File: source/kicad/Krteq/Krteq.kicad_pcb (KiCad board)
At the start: 2 copper layers, 228.6 x 116.3 mm, 263 parts, among them Q1 Q_NMOS_GSD, Q2 Q_NMOS_GSD, Q3 Q_NMOS_GSD, Q4 Q_NMOS_GSD, SW1 Switch, SW10 Switch, SW11 Switch, SW12 Switch, SW13 Switch, SW14 Switch, SW15 Switch, SW16 Switch, SW17 Switch, SW18 Switch, SW19 Switch, SW2 Switch, SW20 Switch, SW21 Switch, SW22 Switch, SW23 Switch, SW24 Switch, SW25 Switch, SW26 Switch, SW27 Switch, SW28 Switch, SW29 Switch, SW3 Switch, SW30 Switch, SW31 Switch, SW32 Switch, SW33 Switch, SW34 Switch, SW35 Switch, SW36 Switch, SW37 Switch, SW38 Switch, SW39 Switch, SW4 Switch, SW40 Switch, SW41 Switch, SW42 Switch, SW43 Switch, SW44 Switch, SW45 Switch, SW46 Switch, SW47 Switch, SW48 Switch, SW49 Switch, SW5 Switch, SW50 Switch, SW51 Switch, SW52 Switch, SW53 Switch, SW54 Switch, SW55 Switch, SW56 Switch, SW57 Switch, SW58 Switch, SW59 Switch, SW6 Switch, SW60 Switch, SW61 Switch, SW7 Switch, SW8 Switch, SW9 Switch

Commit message: MCU cable distance
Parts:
- moved A1 15.0 mm to (204.7, 95.5)
- moved R10 11.1 mm to (144.5, 79.8), turned to -90 degrees
- moved Q4 8.99 mm to (138.6, 79.8), turned to 180 degrees
- moved R11 4.54 mm to (133.0, 79.8), turned to -90 degrees
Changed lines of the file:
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@@
 	(footprint "Resistor_SMD:R_0603_1608Metric"
 		(layer "B.Cu")
-		(at 128.425 79.548 180)
+		(at 132.9625 79.7855 -90)
 		(descr "Resistor SMD 0603 (1608 Metric), square (rectangular) end terminal, IPC-7351 nominal, (Body size source: IPC-SM-782 page 72, https://www.pcb-3d.com/wordpress/wp-content/uploads/ipc-sm-782a_amendment_1_and_2.pdf), generated with kicad-footprint-generator")
 		(tags "resistor")
 		(property "Reference" "R11"
-			(at 0 1.43 0)
+			(at 0 1.43 90)
 			(layer "B.SilkS")
 			(effects
@@
 		)
 		(property "Value" "10k"
-			(at 0 -1.43 0)
+			(at 0 -1.43 90)
 			(layer "B.Fab")
 			(effects
@@
 		)
 		(property "Datasheet" "~"
-			(at 0 0 0)
+			(at 0 0 90)
 			(layer "B.Fab")
 			(hide yes)
@@
 		)
 		(property "Description" "Resistor"
-			(at 0 0 0)
+			(at 0 0 90)
 			(layer "B.Fab")
 			(hide yes)
@@
 		)
 		(fp_text user "${REFERENCE}"
-			(at 0 0 0)
+			(at 0 0 90)
 			(layer "B.Fab")
 			(effects
@@
 		)
 		(pad "1" smd roundrect
-			(at -0.825 0 180)
+			(at -0.825 0 270)
 			(size 0.8 0.95)
 			(layers "B.Cu" "B.Mask" "B.Paste")
@@
 		)
 		(pad "2" smd roundrect
-			(at 0.825 0 180)
+			(at 0.825 0 270)
 			(size 0.8 0.95)
 			(layers "B.Cu" "B.Mask" "B.Paste")
@@
 	(footprint "Package_TO_SOT_SMD:SOT-23"
 		(layer "B.Cu")
-		(at 130.925 84.548 -90)
+		(at 138.55 79.7855 180)
 		(descr "SOT, 3 Pin (JEDEC TO-236 Var AB https://www.jedec.org/document_search?search_api_views_fulltext=TO-236), generated with kicad-footprint-generator ipc_gullwing_generator.py")
 		(tags "SOT TO_SOT_SMD")
 		(property "Reference" "Q4"
-			(at 0 2.4 90)
+			(at 0 2.4 0)
 			(layer "B.SilkS")
 			(effects
@@
 		)
 		(property "Value" "Q_NMOS_GSD"
-			(at 0 -2.4 90)
+			(at 0 -2.4 0)
 			(layer "B.Fab")
 			(effects
@@
 		)
 		(property "Datasheet" "~"
-			(at 0 0 90)
+			(at 0 0 0)
 			(layer "B.Fab")
 			(hide yes)
@@
 		)
 		(property "Description" "N-MOSFET transistor, gate/source/drain"
-			(at 0 0 90)
+			(at 0 0 0)
 			(layer "B.Fab")
 			(hide yes)
@@
 		(attr smd)
 		(fp_line
-			(start -0.76 1.56)
-			(end 0.76 1.56)
+			(start 0.76 1.56)
+			(end 0.76 0.56)
 			(stroke
 				(width 0.12)
@@
 		)
 		(fp_line
-			(start 0.76 1.56)
-			(end 0.76 0.56)
+			(start 0.76 -0.56)
+			(end 0.76 -1.56)
 			(stroke
 				(width 0.12)
@@
 		)
 		(fp_line
-			(start -0.76 1.51)
-			(end -0.76 1.56)
+			(start 0.76 -1.56)
+			(end -0.76 -1.56)
 			(stroke
 				(width 0.12)
@@
 		)
 		(fp_line
-			(start -0.76 -0.39)
-			(end -0.76 0.39)
+			(start -0.76 1.56)
+			(end 0.76 1.56)
 			(stroke
 				(width 0.12)
@@
 		)
 		(fp_line
-			(start 0.76 -0.56)
-			(end 0.76 -1.56)
+			(start -0.76 1.51)
+			(end -0.76 1.56)
 			(stroke
 				(width 0.12)
@@
 		)
 		(fp_line
-			(start -0.76 -1.56)
-			(end -0.76 -1.51)
+			(start -0.76 -0.39)
+			(end -0.76 0.39)
 			(stroke
 				(width 0.12)
@@
 		)
 		(fp_line
-			(start 0.76 -1.56)
-			(end -0.76 -1.56)
+			(start -0.76 -1.56)
+			(end -0.76 -1.51)
 			(stroke
 				(width 0.12)
@@
 		)
 		(fp_line
-			(start -0.9 1.7)
-			(end 0.9 1.7)
+			(start 1.93 0.55)
+			(end 1.93 -0.55)
 			(stroke
 				(width 0.05)
@@
 		)
 		(fp_line
-			(start 0.9 1.7)
-			(end 0.9 0.55)
+			(start 1.93 -0.55)
+			(end 0.9 -0.55)
 			(stroke
 				(width 0.05)
@@
 		)
 		(fp_line
-			(start -1.93 1.5)
-			(end -0.9 1.5)
+			(start 0.9 1.7)
+			(end 0.9 0.55)
 			(stroke
 				(width 0.05)
@@
 		)
 		(fp_line
-			(start -0.9 1.5)
-			(end -0.9 1.7)
+			(start 0.9 0.55)
+			(end 1.93 0.55)
 			(stroke
 				(width 0.05)
@@
 		)
 		(fp_line
-			(start 0.9 0.55)
-			(end 1.93 0.55)
+			(start 0.9 -0.55)
+			(end 0.9 -1.7)
 			(stroke
 				(width 0.05)
@@
 		)
 		(fp_line
-			(start 1.93 0.55)
-			(end 1.93 -0.55)
+			(start 0.9 -1.7)
+			(end -0.9 -1.7)
 			(stroke
 				(width 0.05)
@@
 		)
 		(fp_line
-			(start -1.93 0.39)
-			(end -1.93 1.5)
+			(start -0.9 1.7)
+			(end 0.9 1.7)
 			(stroke
 				(width 0.05)
@@
 		)
 		(fp_line
-			(start -0.9 0.39)
-			(end -1.93 0.39)
+			(start -0.9 1.5)
+			(end -0.9 1.7)
 			(stroke
 				(width 0.05)
@@
 		)
 		(fp_line
-			(start -1.93 -0.39)
-			(end -0.9 -0.39)
+			(start -0.9 0.39)
+			(end -1.93 0.39)
 			(stroke
 				(width 0.05)
@@
 		)
 		(fp_line
-			(start 0.9 -0.55)
-			(end 0.9 -1.7)
+			(start -0.9 -1.5)
+			(end -1.93 -1.5)
 			(stroke
 				(width 0.05)
@@
 		)
 		(fp_line
-			(start 1.93 -0.55)
-			(end 0.9 -0.55)
+			(start -0.9 -1.7)
+			(end -0.9 -1.5)
 			(stroke
 				(width 0.05)
@@
 		)
 		(fp_line
-			(start -1.93 -1.5)
-			(end -1.93 -0.39)
+			(start -1.93 1.5)
+			(end -0.9 1.5)
 			(stroke
 				(width 0.05)
@@
 		)
 		(fp_line
-			(start -0.9 -1.5)
-			(end -1.93 -1.5)
+			(start -1.93 0.39)
+			(end -1.93 1.5)
 			(stroke
 				(width 0.05)
@@
 		)
 		(fp_line
-			(start -0.9 -1.7)
-			(end -0.9 -1.5)
+			(start -1.93 -0.39)
+			(end -0.9 -0.39)
 			(stroke
 				(width 0.05)
@@
 		)
 		(fp_line
-			(start 0.9 -1.7)
-			(end -0.9 -1.7)
+			(start -1.93 -1.5)
+			(end -1.93 -0.39)
 			(stroke
 				(width 0.05)
@@
 		)
 		(fp_text user "${REFERENCE}"
-			(at 0 0 0)
+			(at 0 0 90)
 			(layer "B.Fab")
 			(effects
@@
 		)
 		(pad "1" smd roundrect
-			(at -0.9375 0.95 270)
+			(at -0.9375 0.95 180)
 			(size 1.475 0.6)
 			(layers "B.Cu" "B.Mask" "B.Paste")
@@
 		)
 		(pad "2" smd roundrect
-			(at -0.9375 -0.95 270)
+			(at -0.9375 -0.95 180)
 			(size 1.475 0.6)
 			(layers "B.Cu" "B.Mask" "B.Paste")
@@
 		)
 		(pad "3" smd roundrect
-			(at 0.9375 0 270)
+			(at 0.9375 0 180)
 			(size 1.475 0.6)
 			(layers "B.Cu" "B.Mask" "B.Paste")
@@
 	(footprint "Resistor_SMD:R_0603_1608Metric"
 		(layer "B.Cu")
-		(at 133.425 79.548)
+		(at 144.503125 79.7855 -90)
 		(descr "Resistor SMD 0603 (1608 Metric), square (rectangular) end terminal, IPC-7351 nominal, (Body size source: IPC-SM-782 page 72, https://www.pcb-3d.com/wordpress/wp-content/uploads/ipc-sm-782a_amendment_1_and_2.pdf), generated with kicad-footprint-generator")
 		(tags "resistor")
 		(property "Reference" "R10"
-			(at 0 1.43 0)
+			(at 0 1.43 90)
 			(layer "B.SilkS")
 			(effects
@@
 		)
 		(property "Value" "470"
-			(at 0 -1.43 0)
+			(at 0 -1.43 90)
 			(layer "B.Fab")
 			(effects
@@
 		)
 		(property "Datasheet" "~"
-			(at 0 0 0)
+			(at 0 0 90)
 			(layer "B.Fab")
 			(hide yes)
@@
 		)
 		(property "Description" "Resistor"
-			(at 0 0 0)
+			(at 0 0 90)
 			(layer "B.Fab")
 			(hide yes)
@@
 		(attr smd)
 		(fp_line
-			(start -0.237258 -0.5225)
-			(end 0.237258 -0.5225)
+			(start -0.237258 0.5225)
+			(end 0.237258 0.5225)
 			(stroke
 				(width 0.12)
@@
 		)
 		(fp_line
-			(start -0.237258 0.5225)
-			(end 0.237258 0.5225)
+			(start -0.237258 -0.5225)
+			(end 0.237258 -0.5225)
 			(stroke
 				(width 0.12)
@@
 		)
 		(fp_text user "${REFERENCE}"
-			(at 0 0 0)
+			(at 0 0 90)
 			(layer "B.Fab")
 			(effects
@@
 		)
 		(pad "1" smd roundrect
-			(at -0.825 0)
+			(at -0.825 0 270)
 			(size 0.8 0.95)
 			(layers "B.Cu" "B.Mask" "B.Paste")
@@
 		)
 		(pad "2" smd roundrect
-			(at 0.825 0)
+			(at 0.825 0 270)
 			(size 0.8 0.95)
 			(layers "B.Cu" "B.Mask" "B.Paste")
@@
 	(footprint "Module:RaspberryPi_Pico_Common_THT"
 		(layer "B.Cu")
-		(at 189.66 95.464373 90)
+		(at 204.66 95.464373 90)
 		(descr "Raspberry Pi Pico common (Pico & Pico W) through-hole footprint, supports Raspberry Pi Pico 2, default socketed model has height of 8.51mm, https://datasheets.raspberrypi.com/pico/pico-datasheet.pdf")
 		(tags "module usb pcb antenna")
@@
 			(polygon
 				(pts
-					(xy 140.540105 88.974373) (xy 144.190105 93.674373) (xy 148.53 93.674373) (xy 148.53 79.474373)
-					(xy 144.190105 79.474373) (xy 140.540105 84.174373) (xy 139.53 84.174373) (xy 139.53 88.974373)
+					(xy 155.540105 88.974373) (xy 159.190105 93.674373) (xy 163.53 93.674373) (xy 163.53 79.474373)
+					(xy 159.190105 79.474373) (xy 155.540105 84.174373) (xy 154.53 84.174373) (xy 154.53 88.974373)
 				)
 			)
@@
 			(polygon
 				(pts
-					(xy 193.23 92.324373) (xy 193.23 90.514373) (xy 192.83 90.514373) (xy 192.83 82.634373) (xy 193.23 82.634373)
-					(xy 193.23 80.824373) (xy 212.73 80.824373) (xy 212.73 92.324373)
+					(xy 208.23 92.324373) (xy 208.23 90.514373) (xy 207.83 90.514373) (xy 207.83 82.634373) (xy 208.23 82.634373)
+					(xy 208.23 80.824373) (xy 227.73 80.824373) (xy 227.73 92.324373)
 				)
 			)

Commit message: footprints
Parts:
- Q1, Q2, Q3, Q4: value Q_NMOS_GSD -> Q NMOS GSD
- R1, R4, R7: value 82 -> 82Ω
- R10, R2, R5, R8: value 470 -> 470Ω
- R100, R101, R102, R103, R104, R105, R106, R107, R108, R109, R110, R111, R112, R113, R114, R115, R116, R117, R118, R119, R120, R121, R122, R123, R124, R125, R65, R66, R67, R68, R69, R70, R71, R72, R73, R74, R75, R76, R77, R78, R79, R80, R81, R82, R83, R84, R85, R86, R87, R88, R89, R90, R91, R92, R93, R94, R95, R96, R97, R98, R99: value 330 -> 330Ω
- R11, R3, R6, R9: value 10k -> 10kΩ

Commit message: tweaks
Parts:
- moved Q4 1.50 mm to (138.6, 81.3)
- moved R10 1.50 mm to (144.5, 81.3)
- moved R11 1.50 mm to (133.0, 81.3)
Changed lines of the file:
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@@
 	(footprint "Resistor_SMD:R_0603_1608Metric"
 		(layer "B.Cu")
-		(at 132.9625 79.7855 -90)
+		(at 132.9625 81.2855 -90)
 		(descr "Resistor SMD 0603 (1608 Metric), square (rectangular) end terminal, IPC-7351 nominal, (Body size source: IPC-SM-782 page 72, https://www.pcb-3d.com/wordpress/wp-content/uploads/ipc-sm-782a_amendment_1_and_2.pdf), generated with kicad-footprint-generator")
 		(tags "resistor")
@@
 	(footprint "Package_TO_SOT_SMD:SOT-23"
 		(layer "B.Cu")
-		(at 138.55 79.7855 180)
+		(at 138.55 81.2855 180)
 		(descr "SOT, 3 Pin (JEDEC TO-236 Var AB https://www.jedec.org/document_search?search_api_views_fulltext=TO-236), generated with kicad-footprint-generator ipc_gullwing_generator.py")
 		(tags "SOT TO_SOT_SMD")
@@
 	(footprint "Resistor_SMD:R_0603_1608Metric"
 		(layer "B.Cu")
-		(at 144.503125 79.7855 -90)
+		(at 144.503125 81.2855 -90)
 		(descr "Resistor SMD 0603 (1608 Metric), square (rectangular) end terminal, IPC-7351 nominal, (Body size source: IPC-SM-782 page 72, https://www.pcb-3d.com/wordpress/wp-content/uploads/ipc-sm-782a_amendment_1_and_2.pdf), generated with kicad-footprint-generator")
 		(tags "resistor")

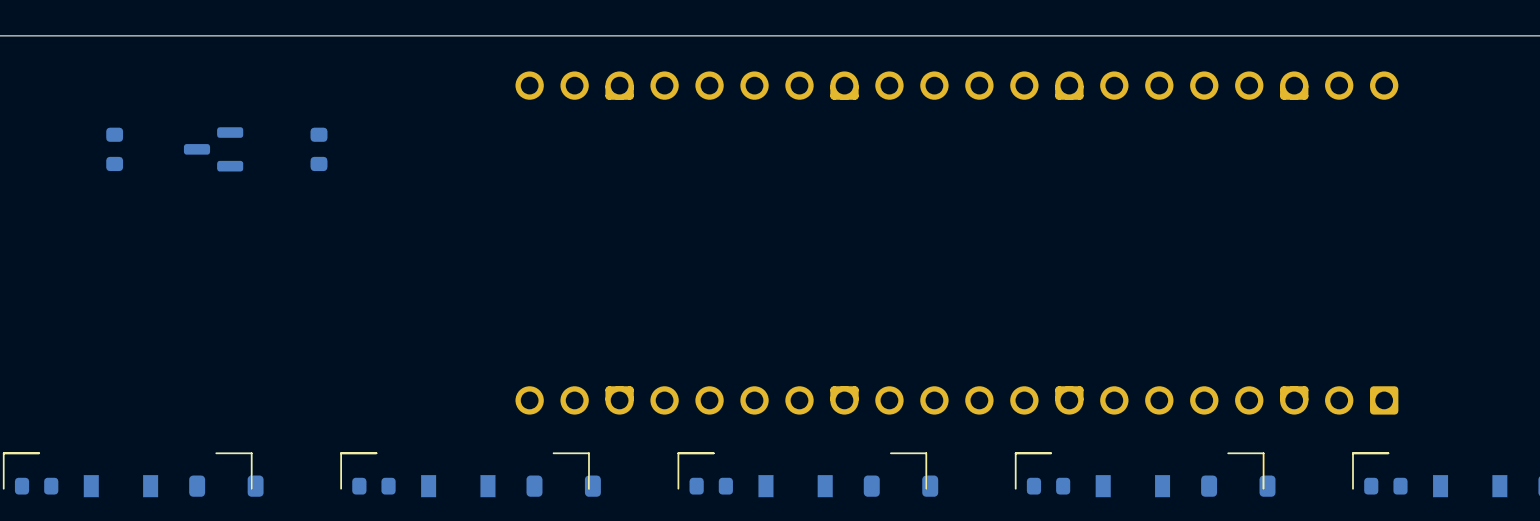
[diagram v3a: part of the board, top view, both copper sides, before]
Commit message: 67cm MCU gap
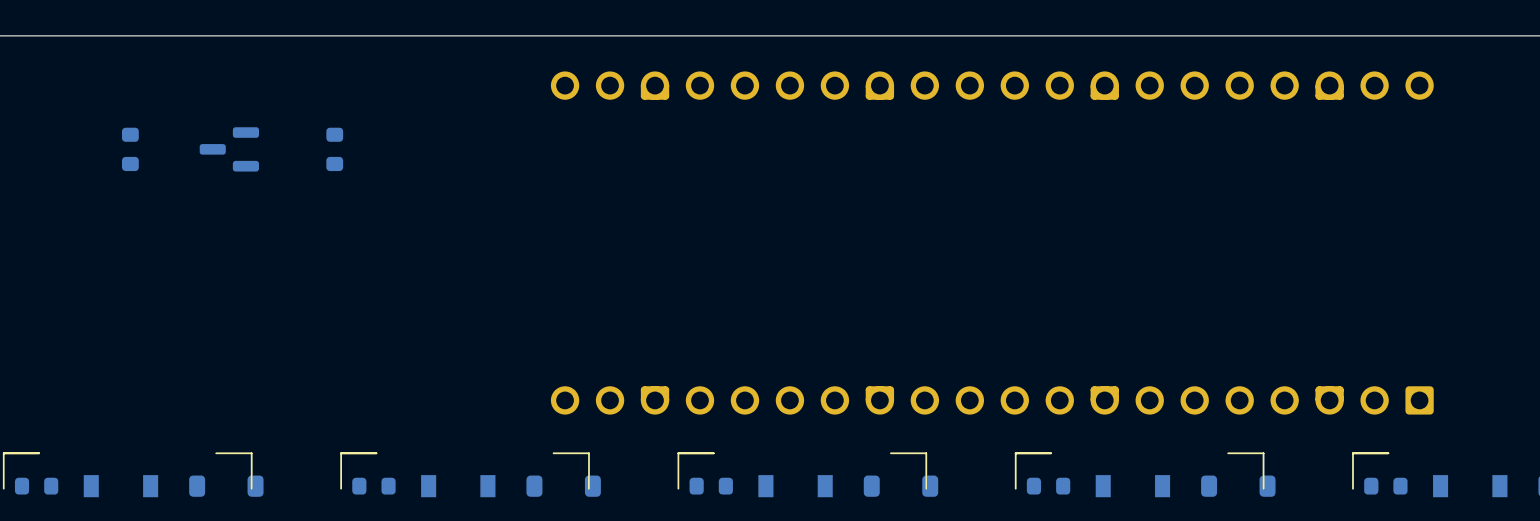
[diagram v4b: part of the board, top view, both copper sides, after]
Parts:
- moved A1 2.00 mm to (206.7, 95.5)
- moved Q4 0.89 mm to (139.4, 81.3)
- moved R10 0.89 mm to (145.4, 81.3)
- moved R11 0.89 mm to (133.9, 81.3)
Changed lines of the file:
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@@
 	(footprint "Resistor_SMD:R_0603_1608Metric"
 		(layer "B.Cu")
-		(at 132.9625 81.2855 -90)
+		(at 133.851724 81.2855 -90)
 		(descr "Resistor SMD 0603 (1608 Metric), square (rectangular) end terminal, IPC-7351 nominal, (Body size source: IPC-SM-782 page 72, https://www.pcb-3d.com/wordpress/wp-content/uploads/ipc-sm-782a_amendment_1_and_2.pdf), generated with kicad-footprint-generator")
 		(tags "resistor")
@@
 	(footprint "Package_TO_SOT_SMD:SOT-23"
 		(layer "B.Cu")
-		(at 138.55 81.2855 180)
+		(at 139.439224 81.2855 180)
 		(descr "SOT, 3 Pin (JEDEC TO-236 Var AB https://www.jedec.org/document_search?search_api_views_fulltext=TO-236), generated with kicad-footprint-generator ipc_gullwing_generator.py")
 		(tags "SOT TO_SOT_SMD")
@@
 	(footprint "Resistor_SMD:R_0603_1608Metric"
 		(layer "B.Cu")
-		(at 144.503125 81.2855 -90)
+		(at 145.392349 81.2855 -90)
 		(descr "Resistor SMD 0603 (1608 Metric), square (rectangular) end terminal, IPC-7351 nominal, (Body size source: IPC-SM-782 page 72, https://www.pcb-3d.com/wordpress/wp-content/uploads/ipc-sm-782a_amendment_1_and_2.pdf), generated with kicad-footprint-generator")
 		(tags "resistor")
@@
 	(footprint "Module:RaspberryPi_Pico_Common_THT"
 		(layer "B.Cu")
-		(at 204.66 95.464373 90)
+		(at 206.66 95.464373 90)
 		(descr "Raspberry Pi Pico common (Pico & Pico W) through-hole footprint, supports Raspberry Pi Pico 2, default socketed model has height of 8.51mm, https://datasheets.raspberrypi.com/pico/pico-datasheet.pdf")
 		(tags "module usb pcb antenna")
@@
 			(polygon
 				(pts
-					(xy 155.540105 88.974373) (xy 159.190105 93.674373) (xy 163.53 93.674373) (xy 163.53 79.474373)
-					(xy 159.190105 79.474373) (xy 155.540105 84.174373) (xy 154.53 84.174373) (xy 154.53 88.974373)
+					(xy 157.540105 88.974373) (xy 161.190105 93.674373) (xy 165.53 93.674373) (xy 165.53 79.474373)
+					(xy 161.190105 79.474373) (xy 157.540105 84.174373) (xy 156.53 84.174373) (xy 156.53 88.974373)
 				)
 			)
@@
 			(polygon
 				(pts
-					(xy 208.23 92.324373) (xy 208.23 90.514373) (xy 207.83 90.514373) (xy 207.83 82.634373) (xy 208.23 82.634373)
-					(xy 208.23 80.824373) (xy 227.73 80.824373) (xy 227.73 92.324373)
+					(xy 210.23 92.324373) (xy 210.23 90.514373) (xy 209.83 90.514373) (xy 209.83 82.634373) (xy 210.23 82.634373)
+					(xy 210.23 80.824373) (xy 229.73 80.824373) (xy 229.73 92.324373)
 				)
 			)

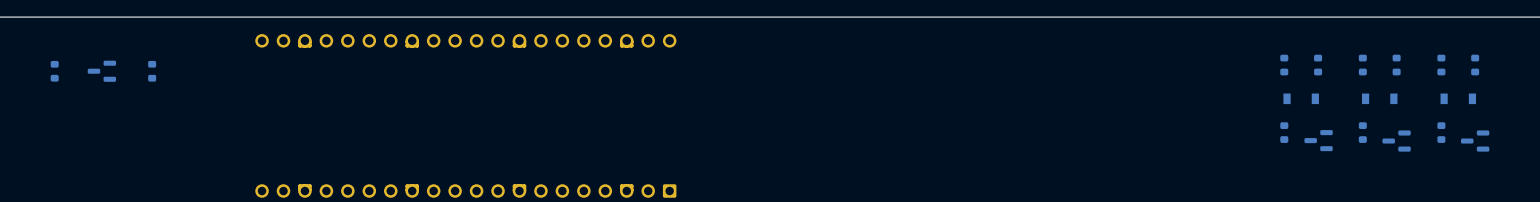
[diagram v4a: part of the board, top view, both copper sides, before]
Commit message: center leds, remove side clips
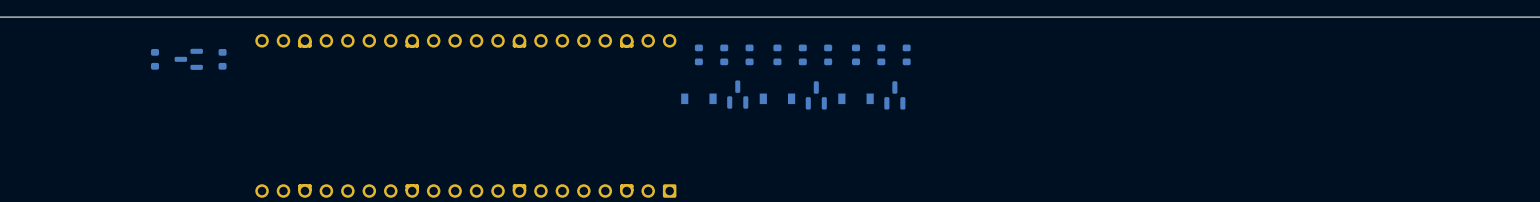
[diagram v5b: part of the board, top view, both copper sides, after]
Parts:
- moved D2 71.3 mm to (219.4, 84.5)
- moved D3 71.3 mm to (210.1, 84.5)
- moved D1 71.3 mm to (228.7, 84.5)
- moved R4 69.9 mm to (219.4, 79.3), turned to 90 degrees
- moved R7 69.9 mm to (210.1, 79.3), turned to 90 degrees
- moved R1 69.9 mm to (228.7, 79.3), turned to 90 degrees
- moved Q3 69.0 mm to (214.7, 84.0), turned to 90 degrees
- moved Q2 68.9 mm to (224.0, 84.1), turned to 90 degrees
- moved Q1 68.9 mm to (233.3, 84.1), turned to 90 degrees
- moved R6 67.3 mm to (225.4, 79.3)
- moved R9 67.3 mm to (216.1, 79.3)
- moved R3 67.3 mm to (234.7, 79.3)
- moved R5 66.3 mm to (222.4, 79.3)
- moved R8 66.3 mm to (213.1, 79.3)
- moved R2 66.3 mm to (231.7, 79.3)
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
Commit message: rework
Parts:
- moved R11 159.5 mm to (305.2, 80.7), turned to 90 degrees
- moved Q4 151.5 mm to (301.2, 80.7), turned to 0 degrees
- moved R10 143.5 mm to (297.2, 80.7), turned to 90 degrees
- moved A1 40.5 mm to (243.0, 77.6), turned to -90 degrees
- moved Q1 27.8 mm to (205.6, 82.2), turned to -90 degrees
- moved R3 25.7 mm to (209.1, 81.7), turned to -90 degrees
- moved R1 24.0 mm to (205.6, 85.7), turned to 180 degrees
- moved R2 20.2 mm to (211.6, 81.7)
- moved D3 18.6 mm to (228.7, 85.7)
- moved D1 18.6 mm to (210.1, 85.7)
- moved R8 17.3 mm to (230.2, 81.7)
- moved R7 15.5 mm to (224.2, 85.7), turned to 180 degrees
- moved R9 11.8 mm to (227.7, 81.7), turned to -90 degrees
- moved Q3 9.67 mm to (224.2, 82.2), turned to -90 degrees
- moved Q2 9.29 mm to (214.9, 82.2), turned to -90 degrees
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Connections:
- A1 pad 1: COL6 -> SIG2
- A1 pad 11: COL3 -> unconnected-(A1-GPIO8-Pad11)
- A1 pad 12: COL2 -> unconnected-(A1-GPIO9-Pad12)
- A1 pad 14: COL1 -> ROW3
- A1 pad 15: COL0 -> ROW4
- A1 pad 16: ROW0 -> ROW5
- A1 pad 17: ROW1 -> COL10
- A1 pad 19: ROW2 -> COL11
- A1 pad 2: COL7 -> SIG3
- A1 pad 20: ROW3 -> BL PWM
- A1 pad 21: BL PWM -> ROW0
- A1 pad 22: unconnected-(A1-GPIO17-Pad22) -> ROW1
- A1 pad 24: ROW4 -> ROW2
- A1 pad 25: ROW5 -> unconnected-(A1-GPIO19-Pad25)
- A1 pad 26: SIG3 -> unconnected-(A1-GPIO20-Pad26)
- A1 pad 27: SIG2 -> COL9
- A1 pad 29: SIG1 -> COL5
- A1 pad 31: unconnected-(A1-GPIO26_ADC0-Pad31) -> COL6
- A1 pad 32: unconnected-(A1-GPIO27_ADC1-Pad32) -> COL7
- A1 pad 34: unconnected-(A1-GPIO28_ADC2-Pad34) -> COL8
- A1 pad 4: COL8 -> SIG1
- A1 pad 5: COL9 -> COL0
- A1 pad 6: COL10 -> COL1
- A1 pad 7: COL11 -> COL2
- A1 pad 9: COL5 -> COL3
